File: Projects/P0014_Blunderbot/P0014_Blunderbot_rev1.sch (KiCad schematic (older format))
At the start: 20 parts, among them J1 22-03-5035, J2 22-03-5035, J3 70553-0037, J4 70553-0037, J5 CONN_01X04, J6 CONN_01X04, P1 CONN_02X03, U1 TC7W241FUTE12LF, U2 MIC5219-5.0YM5-TR, U3 MIC5219-5.0YM5-TR, U4 ATTINY841-SSU

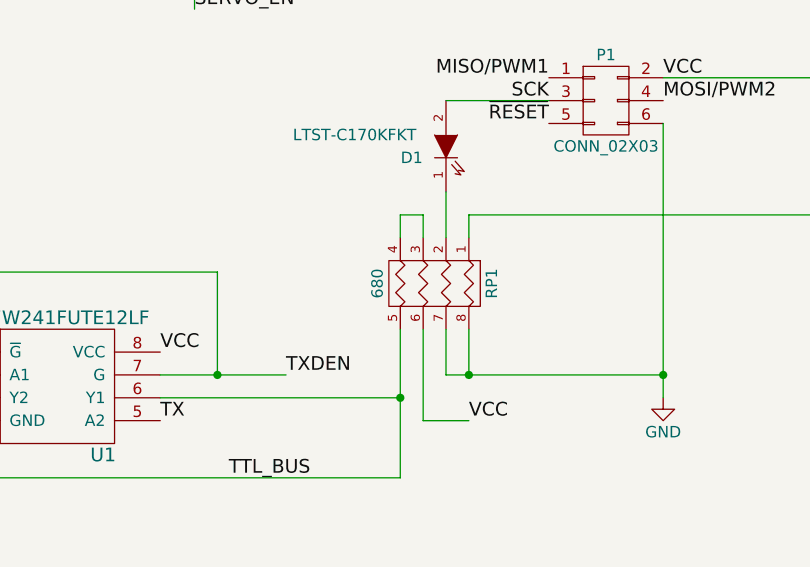
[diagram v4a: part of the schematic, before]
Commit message: layout first pass finished, need to update gerbers for seeed
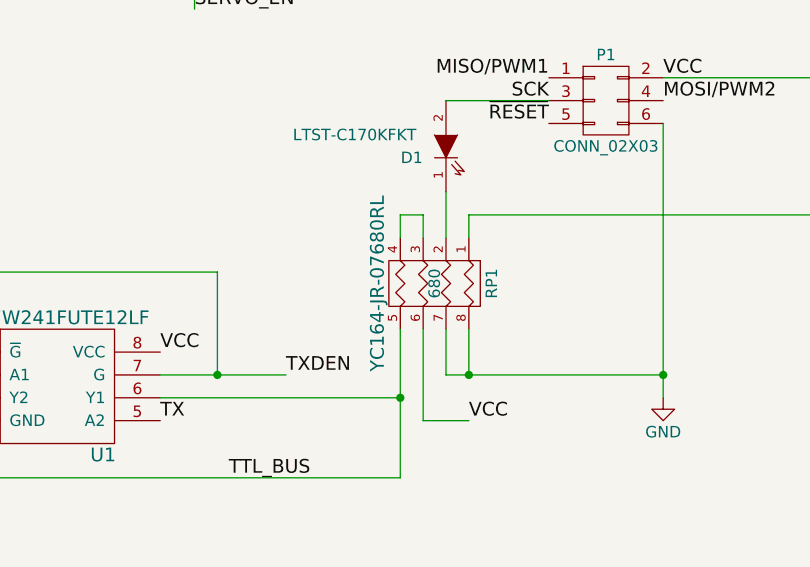
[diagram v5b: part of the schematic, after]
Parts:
- RP1: Part1 (none) -> YC164-JR-07680RL
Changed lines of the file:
@@
 Data
 89 50 4E 47 0D 0A 1A 0A 00 00 00 0D 49 48 44 52 00 00 00 84 00 00 00 84 08 03 00 00 00 66 9A 73
-95 00 00 00 03 73 42 49 54 08 08 08 DB E1 4F E0 00 00 01 71 50 4C 54 45 02 00 00 5B 5B 5C 2B 2B
+95 00 00 00 03 73 42 49 54 08 08 08 DB E1 4F E0 00 00 01 71 50 4C 54 45 01 00 00 5B 5B 5C 2B 2B
 2B 22 07 09 34 0A 0E 3A 0B 0F 29 25 25 2B 09 0C 24 0B 0D 34 34 34 68 67 68 3A 3A 3B 4C 0D 13 6B
 12 1B 9C 1A 26 B4 1D 2C BF 1E 2E 7F 16 20 63 64 64 AB 1C 2A 8E 18 23 64 11 19 3E 0B 10 1E 13 14
@@
 1C 3E 3F 40 4E 51 53 6F 6F 70 80 7F 80 0F 10 10 2E 2F 30 0F 0F 10 57 5A 5C E0 DF E0 46 4A 4C 17
 18 18 5C 5E 60 B7 B8 B9 BE BE C0 1F 1F 20 8F 8F 90 1D 0B 0C 27 28 29 1E 0F 10 46 47 48 26 1F 20
-2F 30 31 37 38 39 75 73 74 78 36 5E 62 00 00 00 01 74 52 4E 53 00 40 E6 D8 66 00 00 15 0B 49 44
+2F 30 31 37 38 39 75 73 74 DC 64 69 7C 00 00 00 01 74 52 4E 53 00 40 E6 D8 66 00 00 15 0B 49 44
 41 54 78 9C BD 5C 89 43 DA CA D6 57 5C 30 B2 16 C4 85 BA 57 45 6D 4B AD 20 54 33 2C B5 22 8B 95
 0C 52 54 52 4B 31 54 11 2B B6 F4 F5 76 F9 FE FA EF CC 4C 42 16 02 F6 F2 EE 7D A7 6A 60 92 CC F9
@@
 AA 3A 6B 5E F4 95 4C FE 1D FA A9 32 D3 19 7D E8 45 BB BD 3F FF FC B7 88 B3 FA 26 A8 E8 67 96 74
 ED F2 03 04 D7 8C BD EF F7 21 FF 16 CD 72 7F D9 E7 1D 06 27 B8 66 9F 98 F0 8D 4C 71 83 E6 F7 FC
-AF 68 BC EF FF 0B E4 FF 01 8C 6E BB 14 85 49 1E 74 00 00 00 00 49 45 4E 44 AE 42 60 82 73
+AF 68 BC EF FF 0B E4 FF 01 8C 6E BB 14 85 49 1E 74 00 00 00 00 49 45 4E 44 AE 42 60 82 06
 EndData
 $EndBitmap
@@
 P 3900 5700
 F 0 "RP1" H 3900 6150 50  0000 C CNN
-F 1 "680" H 3900 5650 50  0000 C CNN
+F 1 "680" H 3900 5900 50  0000 C CNN
 F 2 "Resistors_SMD:R_Array_Convex_4x1206" H 3900 5700 50  0001 C CNN
 F 3 "" H 3900 5700 50  0000 C CNN
+F 4 "YC164-JR-07680RL" H 3900 5650 60  0000 C CNN "Part1"
 	1    3900 5700
 	0    1    1    0

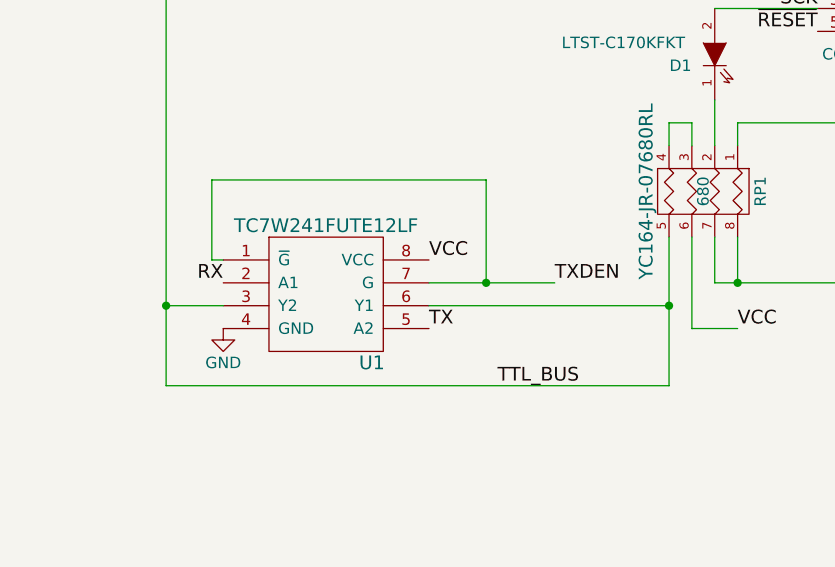
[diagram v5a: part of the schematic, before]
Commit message: finishing routing on bus adapter
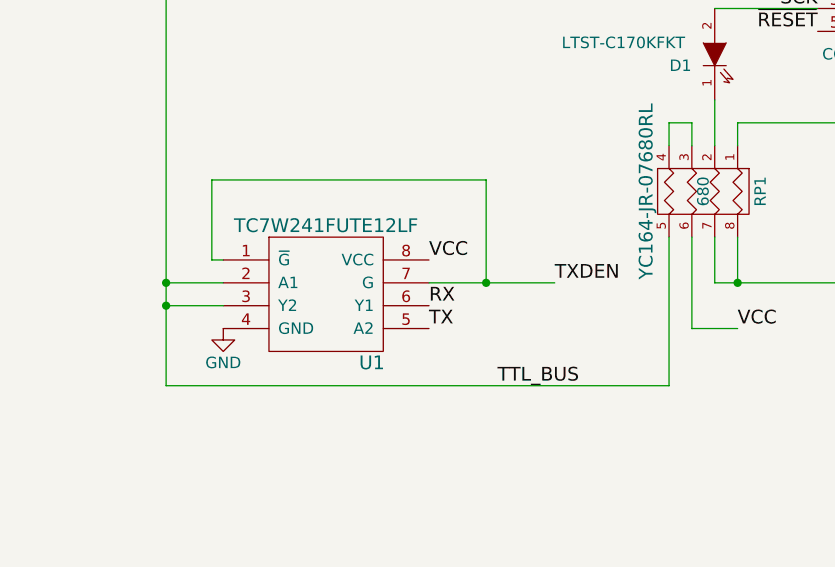
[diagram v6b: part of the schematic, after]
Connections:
- net RX: now also U1.6 (Y1); no longer U1.2 (A1)
- net TTL_BUS: now also U1.2 (A1); no longer U1.6 (Y1)
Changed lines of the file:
@@
 LIBS:valves
 LIBS:open_robotics
+LIBS:macrofab
 LIBS:P0014_Blunderbot_rev1-cache
 EELAYER 25 0
@@
 Data
 89 50 4E 47 0D 0A 1A 0A 00 00 00 0D 49 48 44 52 00 00 00 84 00 00 00 84 08 03 00 00 00 66 9A 73
-95 00 00 00 03 73 42 49 54 08 08 08 DB E1 4F E0 00 00 01 71 50 4C 54 45 01 00 00 5B 5B 5C 2B 2B
+95 00 00 00 03 73 42 49 54 08 08 08 DB E1 4F E0 00 00 01 71 50 4C 54 45 02 00 00 5B 5B 5C 2B 2B
 2B 22 07 09 34 0A 0E 3A 0B 0F 29 25 25 2B 09 0C 24 0B 0D 34 34 34 68 67 68 3A 3A 3B 4C 0D 13 6B
 12 1B 9C 1A 26 B4 1D 2C BF 1E 2E 7F 16 20 63 64 64 AB 1C 2A 8E 18 23 64 11 19 3E 0B 10 1E 13 14
@@
 1C 3E 3F 40 4E 51 53 6F 6F 70 80 7F 80 0F 10 10 2E 2F 30 0F 0F 10 57 5A 5C E0 DF E0 46 4A 4C 17
 18 18 5C 5E 60 B7 B8 B9 BE BE C0 1F 1F 20 8F 8F 90 1D 0B 0C 27 28 29 1E 0F 10 46 47 48 26 1F 20
-2F 30 31 37 38 39 75 73 74 DC 64 69 7C 00 00 00 01 74 52 4E 53 00 40 E6 D8 66 00 00 15 0B 49 44
+2F 30 31 37 38 39 75 73 74 78 36 5E 62 00 00 00 01 74 52 4E 53 00 40 E6 D8 66 00 00 15 0B 49 44
 41 54 78 9C BD 5C 89 43 DA CA D6 57 5C 30 B2 16 C4 85 BA 57 45 6D 4B AD 20 54 33 2C B5 22 8B 95
 0C 52 54 52 4B 31 54 11 2B B6 F4 F5 76 F9 FE FA EF CC 4C 42 16 02 F6 F2 EE 7D A7 6A 60 92 CC F9
@@
 AA 3A 6B 5E F4 95 4C FE 1D FA A9 32 D3 19 7D E8 45 BB BD 3F FF FC B7 88 B3 FA 26 A8 E8 67 96 74
 ED F2 03 04 D7 8C BD EF F7 21 FF 16 CD 72 7F D9 E7 1D 06 27 B8 66 9F 98 F0 8D 4C 71 83 E6 F7 FC
-AF 68 BC EF FF 0B E4 FF 01 8C 6E BB 14 85 49 1E 74 00 00 00 00 49 45 4E 44 AE 42 60 82 06
+AF 68 BC EF FF 0B E4 FF 01 8C 6E BB 14 85 49 1E 74 00 00 00 00 49 45 4E 44 AE 42 60 82 CF
 EndData
 $EndBitmap
@@
 Wire Wire Line
 	1850 2200 1850 4050
-Text Label 2000 6100 2    60   ~ 0
+Text Label 2900 6200 0    60   ~ 0
 RX
 Text Label 2900 6300 0    60   ~ 0
@@
 Text Label 3450 6100 0    60   ~ 0
 TXDEN
-Wire Wire Line
-	2900 6200 3950 6200
 Wire Wire Line
 	3950 5900 3950 6550
@@
 Connection ~ 5100 6100
 Connection ~ 4250 6100
-Connection ~ 3950 6200
 Wire Wire Line
 	3950 5400 4050 5400
@@
 Wire Wire Line
 	8950 3450 7800 3450
+Wire Wire Line
+	2000 6100 1750 6100
+Connection ~ 1750 6100
 $EndSCHEMATC

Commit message: revised P0008, added gerbers
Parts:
- RP1: value 680 -> YC164-JR-07680RL
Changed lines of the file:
@@
 Data
 89 50 4E 47 0D 0A 1A 0A 00 00 00 0D 49 48 44 52 00 00 00 84 00 00 00 84 08 03 00 00 00 66 9A 73
-95 00 00 00 03 73 42 49 54 08 08 08 DB E1 4F E0 00 00 01 71 50 4C 54 45 02 00 00 5B 5B 5C 2B 2B
+95 00 00 00 03 73 42 49 54 08 08 08 DB E1 4F E0 00 00 01 71 50 4C 54 45 01 00 00 5B 5B 5C 2B 2B
 2B 22 07 09 34 0A 0E 3A 0B 0F 29 25 25 2B 09 0C 24 0B 0D 34 34 34 68 67 68 3A 3A 3B 4C 0D 13 6B
 12 1B 9C 1A 26 B4 1D 2C BF 1E 2E 7F 16 20 63 64 64 AB 1C 2A 8E 18 23 64 11 19 3E 0B 10 1E 13 14
@@
 1C 3E 3F 40 4E 51 53 6F 6F 70 80 7F 80 0F 10 10 2E 2F 30 0F 0F 10 57 5A 5C E0 DF E0 46 4A 4C 17
 18 18 5C 5E 60 B7 B8 B9 BE BE C0 1F 1F 20 8F 8F 90 1D 0B 0C 27 28 29 1E 0F 10 46 47 48 26 1F 20
-2F 30 31 37 38 39 75 73 74 78 36 5E 62 00 00 00 01 74 52 4E 53 00 40 E6 D8 66 00 00 15 0B 49 44
+2F 30 31 37 38 39 75 73 74 DC 64 69 7C 00 00 00 01 74 52 4E 53 00 40 E6 D8 66 00 00 15 0B 49 44
 41 54 78 9C BD 5C 89 43 DA CA D6 57 5C 30 B2 16 C4 85 BA 57 45 6D 4B AD 20 54 33 2C B5 22 8B 95
 0C 52 54 52 4B 31 54 11 2B B6 F4 F5 76 F9 FE FA EF CC 4C 42 16 02 F6 F2 EE 7D A7 6A 60 92 CC F9
@@
 AA 3A 6B 5E F4 95 4C FE 1D FA A9 32 D3 19 7D E8 45 BB BD 3F FF FC B7 88 B3 FA 26 A8 E8 67 96 74
 ED F2 03 04 D7 8C BD EF F7 21 FF 16 CD 72 7F D9 E7 1D 06 27 B8 66 9F 98 F0 8D 4C 71 83 E6 F7 FC
-AF 68 BC EF FF 0B E4 FF 01 8C 6E BB 14 85 49 1E 74 00 00 00 00 49 45 4E 44 AE 42 60 82 CF
+AF 68 BC EF FF 0B E4 FF 01 8C 6E BB 14 85 49 1E 74 00 00 00 00 49 45 4E 44 AE 42 60 82 FA
 EndData
 $EndBitmap
@@
 P 3900 5700
 F 0 "RP1" H 3900 6150 50  0000 C CNN
-F 1 "680" H 3900 5900 50  0000 C CNN
+F 1 "YC164-JR-07680RL" H 3900 5650 60  0000 C CNN
 F 2 "Resistors_SMD:R_Array_Convex_4x1206" H 3900 5700 50  0001 C CNN
 F 3 "" H 3900 5700 50  0000 C CNN
-F 4 "YC164-JR-07680RL" H 3900 5650 60  0000 C CNN "Part1"
+F 4 "YC164-JR-07680RL" H 3900 5650 60  0001 C CNN "Part1"
 	1    3900 5700
 	0    1    1    0

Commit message: did some updates I guess?
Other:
- note added: "Notes for next rev\n----------------------\nImprove pin 1 marking for ICs\nMove vias of silkscreen text"
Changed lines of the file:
@@
 Data
 89 50 4E 47 0D 0A 1A 0A 00 00 00 0D 49 48 44 52 00 00 00 84 00 00 00 84 08 03 00 00 00 66 9A 73
-95 00 00 00 03 73 42 49 54 08 08 08 DB E1 4F E0 00 00 01 71 50 4C 54 45 01 00 00 5B 5B 5C 2B 2B
+95 00 00 00 03 73 42 49 54 08 08 08 DB E1 4F E0 00 00 01 71 50 4C 54 45 02 00 00 5B 5B 5C 2B 2B
 2B 22 07 09 34 0A 0E 3A 0B 0F 29 25 25 2B 09 0C 24 0B 0D 34 34 34 68 67 68 3A 3A 3B 4C 0D 13 6B
 12 1B 9C 1A 26 B4 1D 2C BF 1E 2E 7F 16 20 63 64 64 AB 1C 2A 8E 18 23 64 11 19 3E 0B 10 1E 13 14
@@
 1C 3E 3F 40 4E 51 53 6F 6F 70 80 7F 80 0F 10 10 2E 2F 30 0F 0F 10 57 5A 5C E0 DF E0 46 4A 4C 17
 18 18 5C 5E 60 B7 B8 B9 BE BE C0 1F 1F 20 8F 8F 90 1D 0B 0C 27 28 29 1E 0F 10 46 47 48 26 1F 20
-2F 30 31 37 38 39 75 73 74 DC 64 69 7C 00 00 00 01 74 52 4E 53 00 40 E6 D8 66 00 00 15 0B 49 44
+2F 30 31 37 38 39 75 73 74 78 36 5E 62 00 00 00 01 74 52 4E 53 00 40 E6 D8 66 00 00 15 0B 49 44
 41 54 78 9C BD 5C 89 43 DA CA D6 57 5C 30 B2 16 C4 85 BA 57 45 6D 4B AD 20 54 33 2C B5 22 8B 95
 0C 52 54 52 4B 31 54 11 2B B6 F4 F5 76 F9 FE FA EF CC 4C 42 16 02 F6 F2 EE 7D A7 6A 60 92 CC F9
@@
 AA 3A 6B 5E F4 95 4C FE 1D FA A9 32 D3 19 7D E8 45 BB BD 3F FF FC B7 88 B3 FA 26 A8 E8 67 96 74
 ED F2 03 04 D7 8C BD EF F7 21 FF 16 CD 72 7F D9 E7 1D 06 27 B8 66 9F 98 F0 8D 4C 71 83 E6 F7 FC
-AF 68 BC EF FF 0B E4 FF 01 8C 6E BB 14 85 49 1E 74 00 00 00 00 49 45 4E 44 AE 42 60 82 FA
+AF 68 BC EF FF 0B E4 FF 01 8C 6E BB 14 85 49 1E 74 00 00 00 00 49 45 4E 44 AE 42 60 82 A0
 EndData
 $EndBitmap
@@
 	2000 6100 1750 6100
 Connection ~ 1750 6100
+Text Notes 1000 1250 0    60   ~ 0
+Notes for next rev\n----------------------\nImprove pin 1 marking for ICs\nMove vias of silkscreen text
 $EndSCHEMATC
